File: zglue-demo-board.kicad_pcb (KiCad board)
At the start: 2 copper layers, 98 parts, among them J1 0473460001, J10 0473460001, J2 DF13A-2P-1.25H, J3 20021121-00010C4LF, J4 2x20_Header_Female, J5 0473460001, J6 556500488, J7 556500488, J8 WE_686115148922, J9 WE_686115148922, U1 FT232RQ-REEL, U2 NTB0104BQ, U3 NTB0104BQ, U4 NTB0104BQ, U5 93LC56CT-IMC

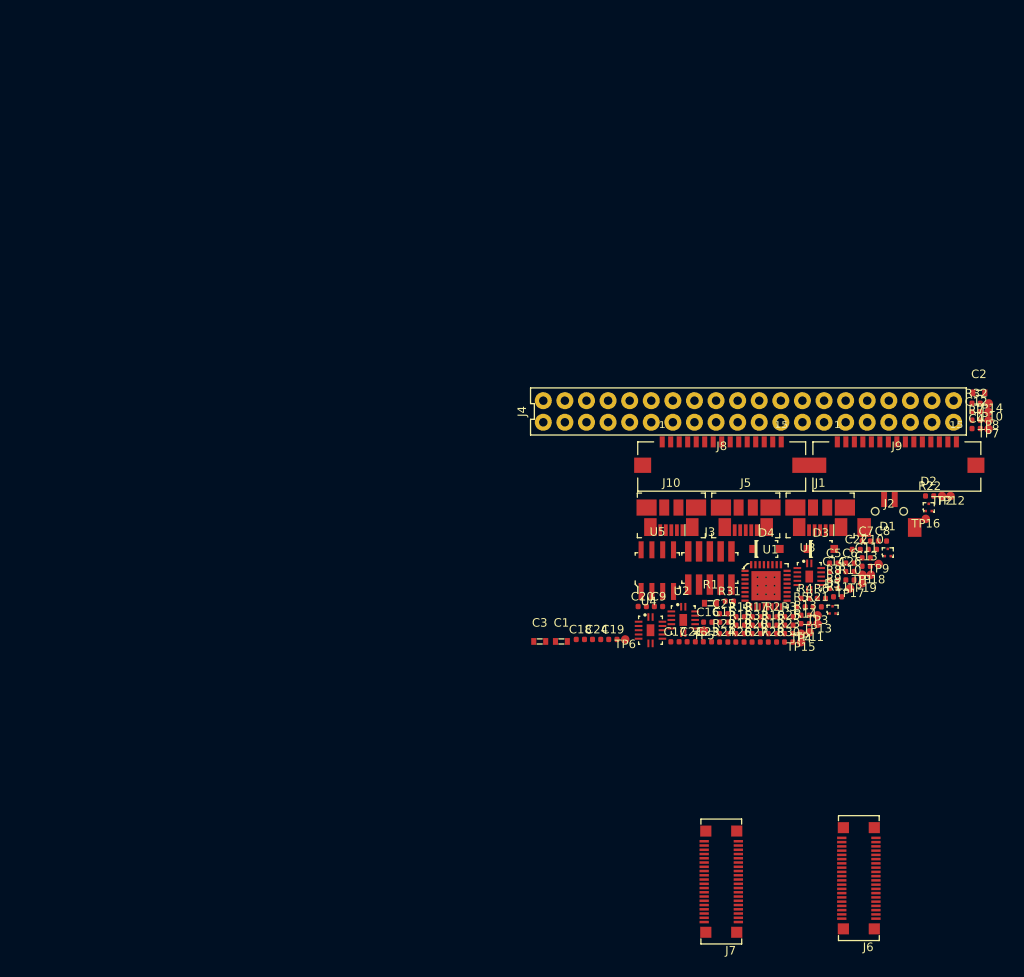
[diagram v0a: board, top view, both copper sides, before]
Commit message: finished initial component placement, some minor changes in schematics related to footprints
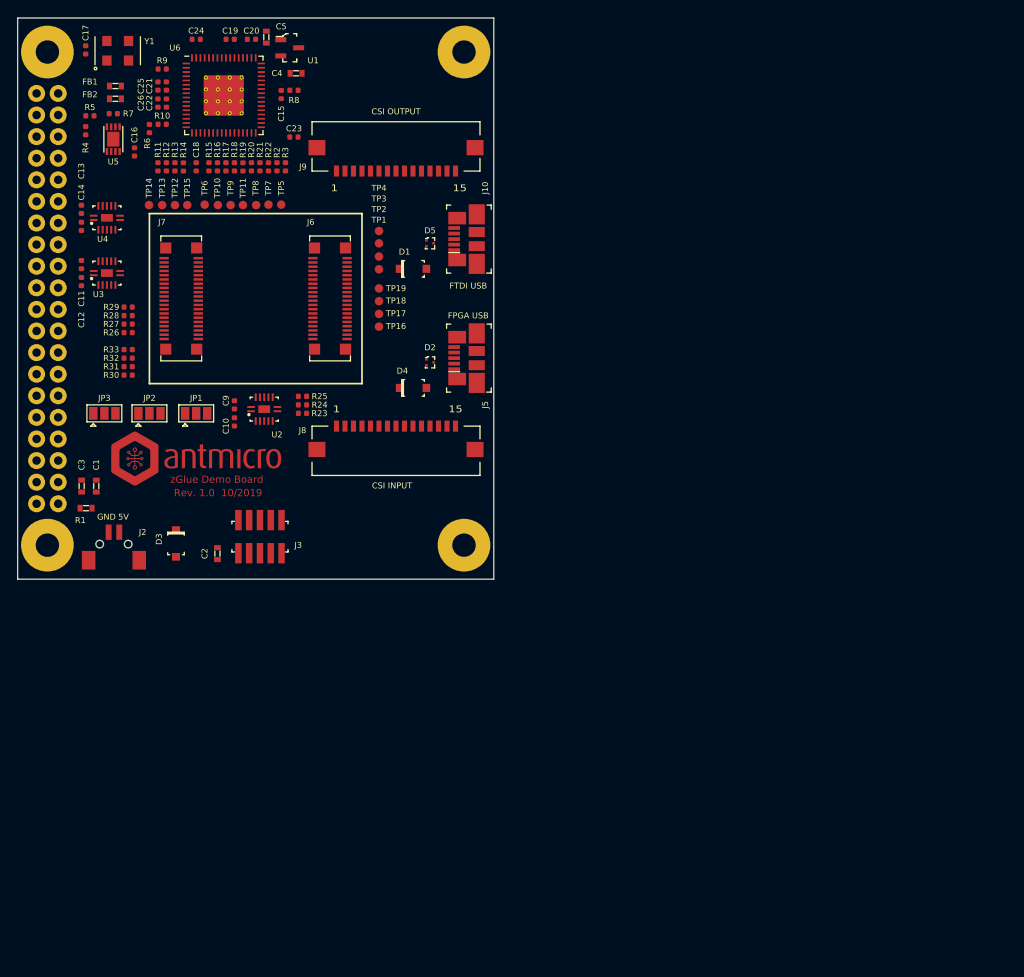
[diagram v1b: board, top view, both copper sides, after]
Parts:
- removed C6: C_47p_0402, antmicro-footprints:0402-cap
- removed C7, C8: C_100n_0402_6V3, antmicro-footprints:0402-cap
- removed J1: 0473460001, antmicro-footprints:USB_Micro_B_Female_0473460001
- added ?: 6-DFN_3x3mm, antmicro-footprints:PAD-6.2mm, F.Cu at (52.5, 62.0)
- added ?: 6-DFN_3x3mm, antmicro-footprints:PAD-6.2mm, F.Cu at (3.50, 62.0)
- added ?: 6-DFN_3x3mm, antmicro-footprints:PAD-6.2mm, F.Cu at (52.5, 4.00)
- added ?: 6-DFN_3x3mm, antmicro-footprints:PAD-6.2mm, F.Cu at (3.50, 4.00)
- added FB1: BLM18AG601SN1D, antmicro-footprints:0603-res, F.Cu at (11.5, 8.00)
- added FB2: BLM18AG601SN1D, antmicro-footprints:0603-res, F.Cu at (11.5, 9.50)
- added JP1: Jumper_3_Open, Jumper:SolderJumper-3_P1.3mm_Open_Pad1.0x1.5mm, F.Cu at (21.0, 46.5)
- added JP2: Jumper_3_Open, Jumper:SolderJumper-3_P1.3mm_Open_Pad1.0x1.5mm, F.Cu at (15.5, 46.5)
- added JP3: Jumper_3_Open, Jumper:SolderJumper-3_P1.3mm_Open_Pad1.0x1.5mm, F.Cu at (10.2, 46.5)
- added N1: antmicro_logo, antmicro-footprints:antmicro-logo_scaled_20mm, F.Cu at (21.0, 52.0)
- added U6: FT4232HQ, antmicro-footprints:FT4232HQ, F.Cu at (24.2, 9.10)
- added Y1: ASFLMB-12.000MHZ-LC-T, antmicro-footprints:ASFLMB, F.Cu at (10.5, 5.00)
- C4: value C_47p_0402 -> C_1u_0603; footprint antmicro-footprints:0402-cap -> antmicro-footprints:0603-cap
- C5: value C_100n_0402_6V3 -> C_1u_0603; footprint antmicro-footprints:0402-cap -> antmicro-footprints:0603-cap
- D1: value TPD2EUSB30DRTR -> MBR0540T1G; footprint antmicro-footprints:SOT-3 -> antmicro-footprints:SOD-123
- J4: moved to B.Cu
- J9: value WE_686115148922 -> WE_686115148922_FLIPPED; footprint antmicro-footprints:WE_686115148922 -> antmicro-footprints:WE_686115148922_FLIPPED
- R2, R3: value R_22R_0402 -> R_0R_0402
- U1: value FT232RQ-REEL -> MCP1700T-3302E_TT; footprint antmicro-footprints:QFN-32-1EP_5x5mm -> antmicro-footprints:SOT-23-3
- U5: footprint antmicro-footprints:SOIC-8_W3.9mm -> antmicro-footprints:DFN-8_2x3mm
- moved R7 107.7 mm to (11.2, 11.2), turned to 180 degrees
- moved J7 107.6 mm to (19.2, 33.0)
- moved J6 106.5 mm to (36.8, 33.0)
- moved C12 106.3 mm to (7.50, 31.0), turned to 90 degrees
- moved R5 101.6 mm to (8.50, 11.5)
- moved TP14 101.4 mm to (15.5, 22.0), turned to 90 degrees
- moved C13 101.4 mm to (7.50, 22.5), turned to 270 degrees
- moved R4 100.9 mm to (8.00, 13.2), turned to 270 degrees
- moved R32 99.9 mm to (13.0, 40.0), turned to 180 degrees
- moved R9 99.8 mm to (17.0, 6.00)
- moved C11 98.5 mm to (7.50, 29.0), turned to 270 degrees
- moved C26 98.3 mm to (16.5, 10.0), turned to 270 degrees
- moved C17 98.2 mm to (8.00, 3.75), turned to 270 degrees
- moved TP12 97.4 mm to (18.6, 22.0), turned to 90 degrees
- moved C14 97.4 mm to (7.50, 24.5), turned to 90 degrees
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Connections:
- C16 pad 1: /3V3_SYS -> /3V3_FTDI
- C17 pad 1: /3V3_SYS -> /3V3_FTDI
- C20 pad 1: /1V8_SYS -> /1V8_FTDI
- C24 pad 1: /1V8_SYS -> /1V8_FTDI
- C4 pad 1: /DBG_USB_D_P -> /5V0_DBG_USB
- C5 pad 1: /1V8_SYS -> /3V3_FTDI
- D2 pad 1: /DBG_USB_D_P -> /USB_D_P
- D2 pad 2: /DBG_USB_D_N -> /USB_D_N
- J10 pad 1: /5V0_USB -> /5V0_DBG_USB
- J10 pad SH: Net-(J10-PadSH) -> GND
- J5 pad 1: /5V0_DBG_USB -> /5V0_USB
- J5 pad 2: /DBG_USB_D_N -> /USB_D_N
- J5 pad 3: /DBG_USB_D_P -> /USB_D_P
- J5 pad SH: Net-(J5-PadSH) -> GND
- R10 pad 1: /3V3_SYS -> /3V3_FTDI
- R15 pad 2: /E_PROC_RST_3V3 -> Net-(R15-Pad2)
- R16 pad 2: Net-(R16-Pad2) -> /E_PROC_RST_3V3
- R2 pad 1: /DBG_TX -> Net-(R2-Pad1)
- R2 pad 2: Net-(R2-Pad2) -> /DBG_RX
- R21 pad 2: /CTRL_RST_FLASH_SOC_CS -> /DONE_3V3
- R22 pad 2: /DONE_3V3 -> /CTRL_RST_FLASH_SOC_CS_3V3
- R23 pad 1: /CTRL_RST -> /CTRL_RST_FLASH_SOC_CS
- R3 pad 2: /DBG_RX -> /DBG_TX
- R4 pad 2: /3V3_SYS -> /3V3_FTDI
- R6 pad 2: /3V3_SYS -> /3V3_FTDI
- R7 pad 2: /3V3_SYS -> /3V3_FTDI
- R8 pad 1: /3V3_SYS -> /3V3_FTDI
- TP5 pad 1: /CTRL_RST_3V3 -> /CTRL_RST_FLASH_SOC_CS_3V3
- U1 pad 1: /1V8_SYS -> GND
- U1 pad 2: Net-(R2-Pad2) -> /3V3_FTDI
- U1 pad 3: Net-(U1-Pad3) -> /5V0_DBG_USB
- U2 pad 13: /CTRL_RST_3V3 -> /CTRL_RST_FLASH_SOC_CS_3V3
- U5 pad 6: /3V3_SYS -> /3V3_FTDI
- U5 pad 8: /3V3_SYS -> /3V3_FTDI
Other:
- board outline added: 56 x 66 mm
- board text added: "5V"
- board text added: "CSI INPUT"
- board text added: "CSI OUTPUT"
- board text added: "FPGA USB"
- board text added: "FTDI USB"
- board text added: "GND"
- board text added: "Rev. 1.0 10/2019"
- board text added: "zGlue Demo Board"

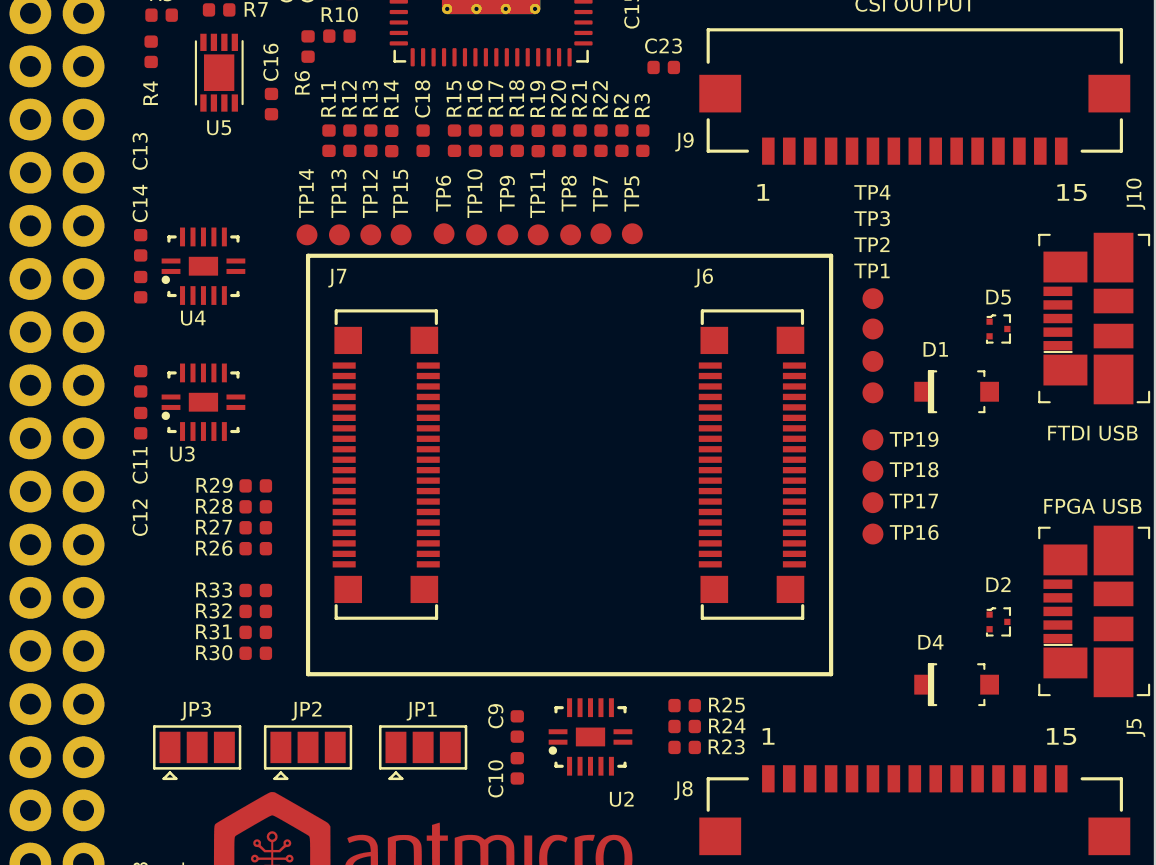
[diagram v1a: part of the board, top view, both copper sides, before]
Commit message: Rotated adapter board footprint by 180 deg
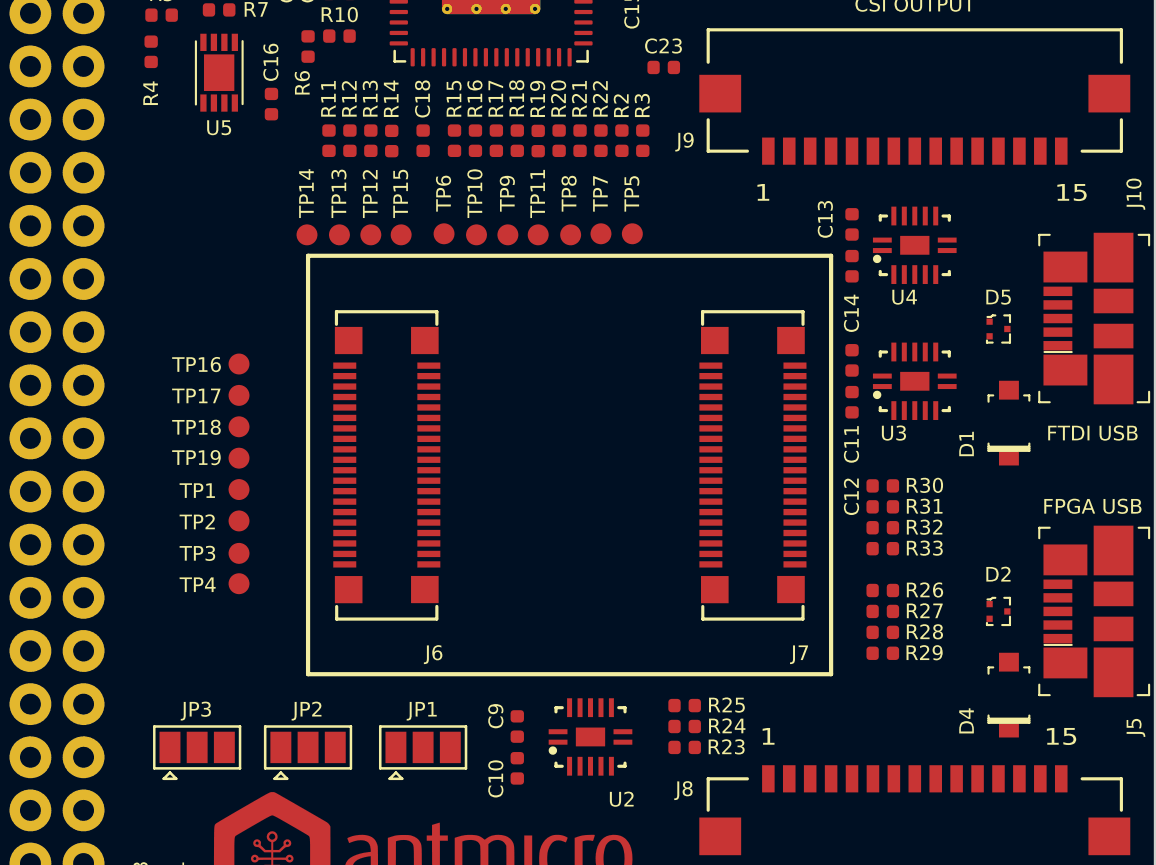
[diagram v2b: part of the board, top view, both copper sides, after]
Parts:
- moved C11 34.0 mm to (41.5, 28.0)
- moved C12 34.0 mm to (41.5, 30.0)
- moved C13 34.0 mm to (41.5, 21.5)
- moved C14 34.0 mm to (41.5, 23.5)
- moved U3 34.0 mm to (44.5, 29.0)
- moved U4 34.0 mm to (44.5, 22.5)
- moved TP4 33.3 mm to (12.2, 38.7), turned to 0 degrees
- moved TP3 32.2 mm to (12.2, 37.3), turned to 0 degrees
- moved TP16 31.3 mm to (12.2, 28.2), turned to 0 degrees
- moved TP2 31.3 mm to (12.2, 35.7), turned to 0 degrees
- moved R29 31.0 mm to (43.0, 42.0), turned to 0 degrees
- moved R30 31.0 mm to (43.0, 34.0), turned to 0 degrees
- moved TP17 30.7 mm to (12.2, 29.7), turned to 0 degrees
- moved TP1 30.7 mm to (12.2, 34.2), turned to 0 degrees
- moved R28 30.6 mm to (43.0, 41.0), turned to 0 degrees
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
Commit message: Finished routing
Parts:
- removed ? (x4): 6-DFN_3x3mm, antmicro-footprints:PAD-6.2mm
- moved R26 1.32 mm to (44.3, 39.0)
- moved R27 1.32 mm to (44.3, 40.0)
- moved R28 1.32 mm to (44.3, 41.0)
- moved R29 1.32 mm to (44.3, 42.0)
- moved R30 1.32 mm to (44.3, 34.0)
- moved R31 1.32 mm to (44.3, 35.0)
- moved R32 1.32 mm to (44.3, 36.0)
- moved R33 1.32 mm to (44.3, 37.0)
- moved C11 0.83 mm to (41.5, 27.2)
- moved C12 0.83 mm to (41.5, 29.2)
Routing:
- net /3V3_SYS: track 0.00 -> 191.1 mm, vias 0 -> 7
- net GND: track 0.00 -> 135.8 mm, vias 0 -> 77
- net /VCCIO3: track 0.00 -> 74.7 mm, vias 0 -> 4
- net /3V3_FTDI: track 0.00 -> 69.4 mm, vias 0 -> 5
- net /VCCIO2: track 0.00 -> 59.6 mm, vias 0 -> 3
- net /PROG_USB_D_N: track 0.00 -> 55.6 mm, vias 0 -> 2
- net /PROG_USB_D_P: track 0.00 -> 53.6 mm, vias 0 -> 2
- net /5V0_DBG_USB: track 0.00 -> 49.2 mm, vias 0 -> 2
- net /VCCIO: track 0.00 -> 48.5 mm, vias 0 -> 5
- net /TCK: track 0.00 -> 42.6 mm, vias 0 -> 2
- net /E_PROC_SCK_3V3: track 0.00 -> 41.9 mm, vias 0 -> 2
- net /TDI: track 0.00 -> 41.4 mm, vias 0 -> 2
- net /TDO: track 0.00 -> 41.4 mm, vias 0 -> 2
- net /CAM_GPIO: track 0.00 -> 40.8 mm, vias 0 -> 2
- net /1V8_SYS: track 0.00 -> 40.7 mm, vias 0 -> 6
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- added copper zone on In4.Cu, net /5V0_IN
- added copper zone on In4.Cu, net /VUSB
- added copper zone on In1.Cu, net GND
- added copper zone on In4.Cu, net GND
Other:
- copper layers 2 -> 6
- net class Default: clearance 0.2 -> 0.125; trace_width 0.25 -> 0.15; via_dia 0.8 -> 0.55; via_drill 0.4 -> 0.15
- rule trace_clearance: 0.2 -> 0.125
- rule trace_min: 0.2 -> 0.15
- rule via_min_drill: 0.3 -> 0.15
- rule via_min_size: 0.4 -> 0.55

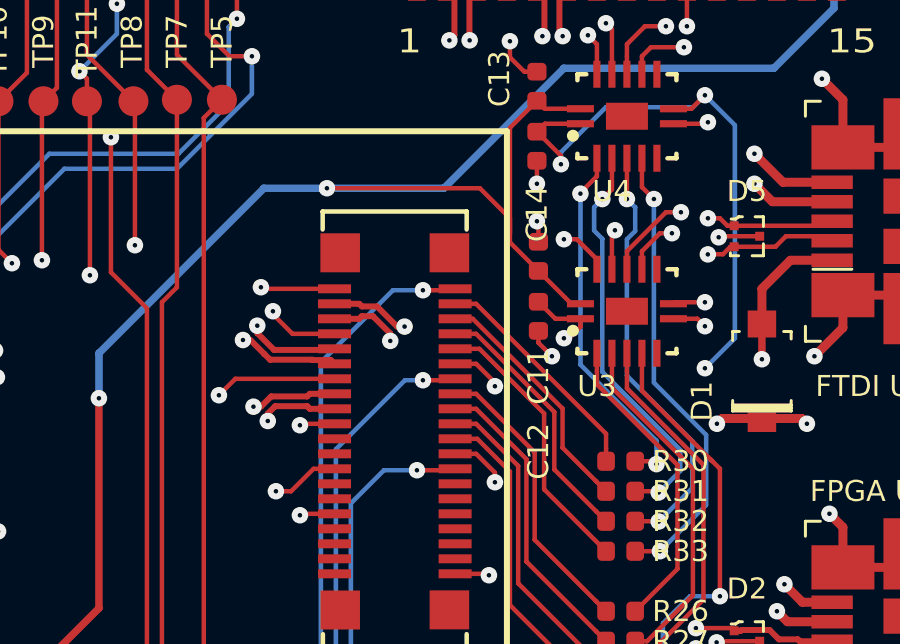
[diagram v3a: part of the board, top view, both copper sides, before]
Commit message: Tuned differential pairs
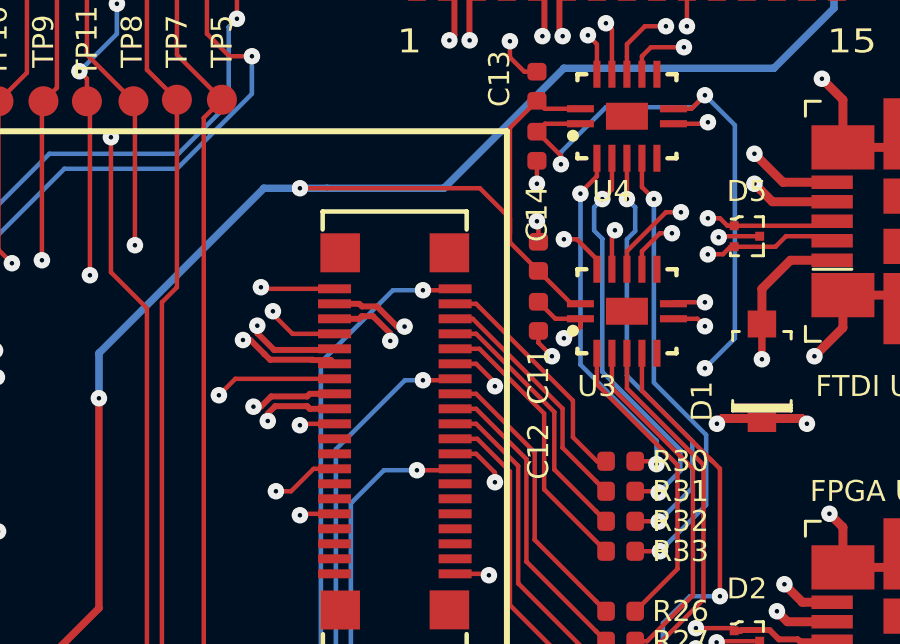
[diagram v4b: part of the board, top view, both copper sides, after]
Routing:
- net /CSI_CLK_OUT_P: track 22.9 -> 28.7 mm
- net /CSI_CLK_OUT_N: track 22.8 -> 28.7 mm
- net /CSI_D2_IN_N: track 32.1 -> 36.6 mm
- net /CSI_D2_IN_P: track 32.6 -> 36.6 mm
- net /CSI_D1_OUT_N: track 23.7 -> 27.7 mm
- net /PROG_USB_D_P: track 53.6 -> 56.8 mm
- net /CSI_D1_IN_N: track 33.5 -> 36.6 mm
- net /CSI_D1_IN_P: track 34.0 -> 36.6 mm
- net /CSI_D1_OUT_P: track 25.2 -> 27.7 mm
- net /CSI_D2_OUT_N: track 26.6 -> 28.2 mm
- net /3V3_SYS: track 191.1 -> 192.0 mm
- net /CSI_CLK_IN_N: track 36.1 -> 36.6 mm
